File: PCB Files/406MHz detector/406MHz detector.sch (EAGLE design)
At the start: 17 parts, among them J1 switch

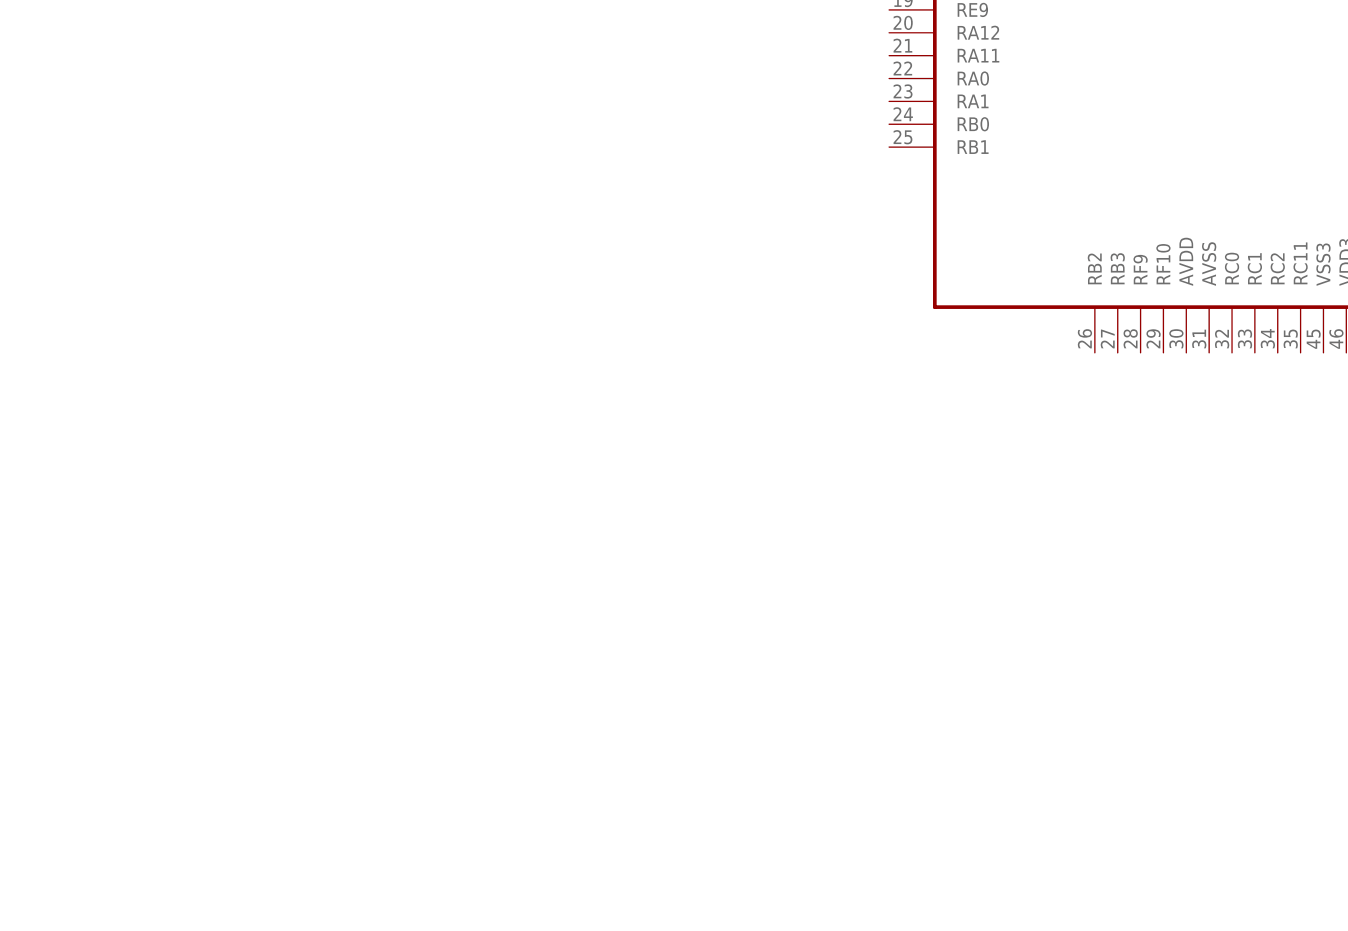
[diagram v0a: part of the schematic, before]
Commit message: added a microcontroller
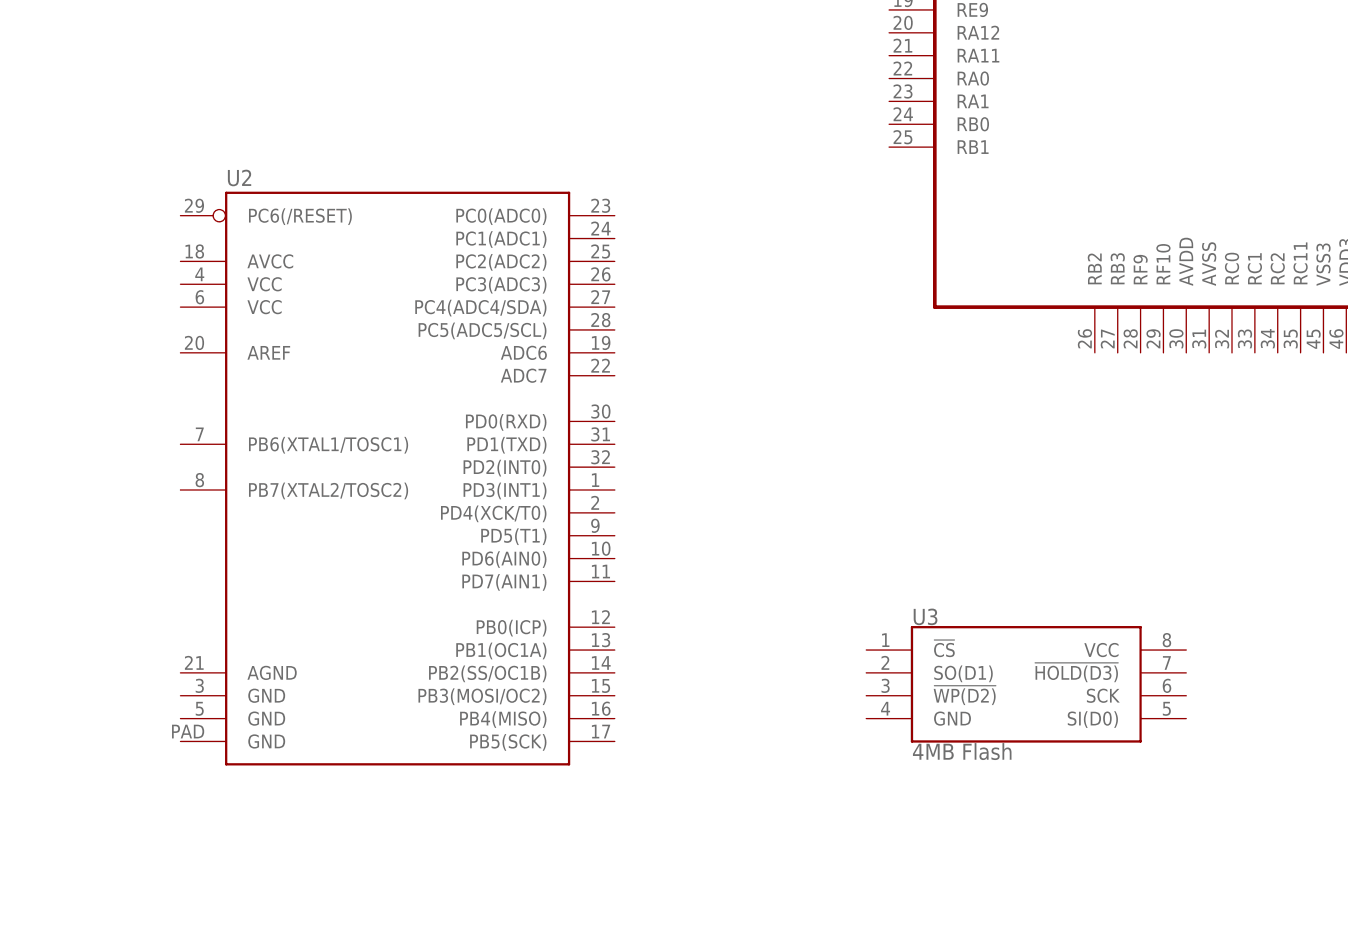
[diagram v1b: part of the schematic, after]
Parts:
- added U2: (no value), SparkFun-IC-Microcontroller:ATMEGA328P_MLFMLF32
- added U3: 4MB Flash, SparkFun-IC-Memory:AT25SF041
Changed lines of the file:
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@@
 <?xml version="1.0" encoding="utf-8"?>
 <!DOCTYPE eagle SYSTEM "eagle.dtd">
-<eagle version="9.3.0">
+<eagle version="9.5.2">
 <drawing>
 <settings>
@@
 <part name="GND6" library="SparkFun-PowerSymbols" library_urn="urn:adsk.eagle:library:530" deviceset="GND2" device="" value="GND"/>
 <part name="GND7" library="SparkFun-PowerSymbols" library_urn="urn:adsk.eagle:library:530" deviceset="GND2" device="" value="GND"/>
+<part name="U2" library="SparkFun-IC-Microcontroller" library_urn="urn:adsk.eagle:library:525" deviceset="ATMEGA328P_MLF" device="MLF32" package3d_urn="urn:adsk.eagle:package:38946/1"/>
+<part name="U3" library="SparkFun-IC-Memory" library_urn="urn:adsk.eagle:library:524" deviceset="AT25SF041" device="" package3d_urn="urn:adsk.eagle:package:38840/1" value="4MB Flash"/>
 </parts>
 <sheets>
@@
 <attribute name="VALUE" x="119.38" y="92.202" size="1.778" layer="96" align="top-center"/>
 </instance>
+<instance part="U2" gate="U$1" x="203.2" y="111.76" smashed="yes">
+<attribute name="NAME" x="185.42" y="140.462" size="1.778" layer="95"/>
+<attribute name="VALUE" x="185.42" y="73.66" size="1.778" layer="96"/>
+</instance>
+<instance part="U3" gate="G$1" x="271.78" y="83.82" smashed="yes">
+<attribute name="NAME" x="261.62" y="91.694" size="1.778" layer="95" font="vector"/>
+<attribute name="VALUE" x="261.62" y="78.486" size="1.778" layer="96" font="vector" align="top-left"/>
+</instance>
 </instances>

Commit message: added some nets
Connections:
- new net N$15: U2.PD0(RXD), U3.!CS
- new net N$16: U2.PD2(INT0), U3.!HOLD(D3), U3.SCK, U3.SI(D0), U3.VCC
- new net N$17: U2.GND@PAD, U3.GND
- new net N$18: U2.PB7(XTAL2/TOSC2), U3.SO(D1)
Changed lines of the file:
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@@
+</segment>
+</net>
+<net name="N$15" class="0">
+<segment>
+<pinref part="U2" gate="U$1" pin="PD0(RXD)"/>
+<pinref part="U3" gate="G$1" pin="!CS"/>
+<wire x1="228.6" y1="114.3" x2="256.54" y2="114.3" width="0.1524" layer="91"/>
+<wire x1="256.54" y1="114.3" x2="256.54" y2="88.9" width="0.1524" layer="91"/>
+</segment>
+</net>
+<net name="N$16" class="0">
+<segment>
+<pinref part="U2" gate="U$1" pin="PD2(INT0)"/>
+<pinref part="U3" gate="G$1" pin="SI(D0)"/>
+<wire x1="228.6" y1="109.22" x2="292.1" y2="109.22" width="0.1524" layer="91"/>
+<wire x1="292.1" y1="109.22" x2="292.1" y2="88.9" width="0.1524" layer="91"/>
+<pinref part="U3" gate="G$1" pin="VCC"/>
+<wire x1="292.1" y1="88.9" x2="292.1" y2="86.36" width="0.1524" layer="91"/>
+<junction x="292.1" y="88.9"/>
+<pinref part="U3" gate="G$1" pin="!HOLD(D3)"/>
+<wire x1="292.1" y1="86.36" x2="292.1" y2="83.82" width="0.1524" layer="91"/>
+<junction x="292.1" y="86.36"/>
+<pinref part="U3" gate="G$1" pin="SCK"/>
+<wire x1="292.1" y1="83.82" x2="292.1" y2="81.28" width="0.1524" layer="91"/>
+<junction x="292.1" y="83.82"/>
+</segment>
+</net>
+<net name="N$17" class="0">
+<segment>
+<pinref part="U3" gate="G$1" pin="GND"/>
+<wire x1="256.54" y1="81.28" x2="256.54" y2="63.5" width="0.1524" layer="91"/>
+<wire x1="256.54" y1="63.5" x2="180.34" y2="63.5" width="0.1524" layer="91"/>
+<pinref part="U2" gate="U$1" pin="GND@PAD"/>
+<wire x1="180.34" y1="63.5" x2="180.34" y2="78.74" width="0.1524" layer="91"/>
+</segment>
+</net>
+<net name="N$18" class="0">
+<segment>
+<pinref part="U2" gate="U$1" pin="PB7(XTAL2/TOSC2)"/>
+<wire x1="180.34" y1="106.68" x2="160.02" y2="106.68" width="0.1524" layer="91"/>
+<wire x1="160.02" y1="106.68" x2="160.02" y2="40.64" width="0.1524" layer="91"/>
+<wire x1="160.02" y1="40.64" x2="246.38" y2="40.64" width="0.1524" layer="91"/>
+<wire x1="246.38" y1="40.64" x2="246.38" y2="86.36" width="0.1524" layer="91"/>
+<pinref part="U3" gate="G$1" pin="SO(D1)"/>
+<wire x1="246.38" y1="86.36" x2="256.54" y2="86.36" width="0.1524" layer="91"/>
 </segment>
 </net>

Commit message: copied from master
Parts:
- removed U2: (no value), SparkFun-IC-Microcontroller:ATMEGA328P_MLFMLF32
- removed U3: 4MB Flash, SparkFun-IC-Memory:AT25SF041
- added D2: (no value), SparkFun-LED:LED_RING
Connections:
- net N$15: now also D2.1, D2.4; no longer U2.PD0(RXD), U3.!CS
- net N$16: now also D2.8, D2.9; no longer U2.PD2(INT0), U3.!HOLD(D3), U3.SCK, U3.SI(D0), U3.VCC
- net N$17: now also D2.12, D2.COM2; no longer U2.GND@PAD, U3.GND
- net N$18: now also D2.COM3; no longer U2.PB7(XTAL2/TOSC2), U3.SO(D1)
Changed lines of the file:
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@@
 <part name="GND6" library="SparkFun-PowerSymbols" library_urn="urn:adsk.eagle:library:530" deviceset="GND2" device="" value="GND"/>
 <part name="GND7" library="SparkFun-PowerSymbols" library_urn="urn:adsk.eagle:library:530" deviceset="GND2" device="" value="GND"/>
-<part name="U2" library="SparkFun-IC-Microcontroller" library_urn="urn:adsk.eagle:library:525" deviceset="ATMEGA328P_MLF" device="MLF32" package3d_urn="urn:adsk.eagle:package:38946/1"/>
-<part name="U3" library="SparkFun-IC-Memory" library_urn="urn:adsk.eagle:library:524" deviceset="AT25SF041" device="" package3d_urn="urn:adsk.eagle:package:38840/1" value="4MB Flash"/>
+<part name="D2" library="SparkFun-LED" library_urn="urn:adsk.eagle:library:529" deviceset="LED_RING" device="" package3d_urn="urn:adsk.eagle:package:39360/1"/>
 </parts>
 <sheets>
 <sheet>
 <plain>
+<wire x1="0" y1="0" x2="0" y2="381" width="0.1524" layer="150"/>
+<wire x1="0" y1="381" x2="508" y2="381" width="0.1524" layer="150"/>
+<wire x1="508" y1="381" x2="508" y2="0" width="0.1524" layer="150"/>
+<wire x1="508" y1="0" x2="0" y2="0" width="0.1524" layer="150"/>
+<wire x1="508" y1="381" x2="1016" y2="381" width="0.1524" layer="150"/>
+<wire x1="1016" y1="381" x2="1016" y2="0" width="0.1524" layer="150"/>
+<wire x1="1016" y1="0" x2="508" y2="0" width="0.1524" layer="150"/>
+<wire x1="1016" y1="381" x2="1524" y2="381" width="0.1524" layer="150"/>
+<wire x1="1524" y1="381" x2="1524" y2="0" width="0.1524" layer="150"/>
+<wire x1="1524" y1="0" x2="1016" y2="0" width="0.1524" layer="150"/>
 </plain>
 <instances>
@@
 <attribute name="VALUE" x="119.38" y="92.202" size="1.778" layer="96" align="top-center"/>
 </instance>
-<instance part="U2" gate="U$1" x="203.2" y="111.76" smashed="yes">
-<attribute name="NAME" x="185.42" y="140.462" size="1.778" layer="95"/>
-<attribute name="VALUE" x="185.42" y="73.66" size="1.778" layer="96"/>
-</instance>
-<instance part="U3" gate="G$1" x="271.78" y="83.82" smashed="yes">
-<attribute name="NAME" x="261.62" y="91.694" size="1.778" layer="95" font="vector"/>
-<attribute name="VALUE" x="261.62" y="78.486" size="1.778" layer="96" font="vector" align="top-left"/>
+<instance part="D2" gate="G$1" x="193.04" y="96.52" smashed="yes">
+<attribute name="VALUE" x="193.04" y="81.026" size="1.778" layer="96" font="vector" align="top-center"/>
+<attribute name="NAME" x="193.04" y="112.014" size="1.778" layer="95" font="vector" align="bottom-center"/>
 </instance>
 </instances>
@@
 <net name="N$15" class="0">
 <segment>
-<pinref part="U2" gate="U$1" pin="PD0(RXD)"/>
-<pinref part="U3" gate="G$1" pin="!CS"/>
-<wire x1="228.6" y1="114.3" x2="256.54" y2="114.3" width="0.1524" layer="91"/>
-<wire x1="256.54" y1="114.3" x2="256.54" y2="88.9" width="0.1524" layer="91"/>
+<pinref part="D2" gate="G$1" pin="1"/>
+<wire x1="177.8" y1="99.06" x2="167.64" y2="99.06" width="0.1524" layer="91"/>
+<wire x1="167.64" y1="99.06" x2="167.64" y2="109.22" width="0.1524" layer="91"/>
+<pinref part="D2" gate="G$1" pin="4"/>
+<wire x1="167.64" y1="109.22" x2="177.8" y2="109.22" width="0.1524" layer="91"/>
 </segment>
 </net>
 <net name="N$16" class="0">
 <segment>
-<pinref part="U2" gate="U$1" pin="PD2(INT0)"/>
-<pinref part="U3" gate="G$1" pin="SI(D0)"/>
-<wire x1="228.6" y1="109.22" x2="292.1" y2="109.22" width="0.1524" layer="91"/>
-<wire x1="292.1" y1="109.22" x2="292.1" y2="88.9" width="0.1524" layer="91"/>
-<pinref part="U3" gate="G$1" pin="VCC"/>
-<wire x1="292.1" y1="88.9" x2="292.1" y2="86.36" width="0.1524" layer="91"/>
-<junction x="292.1" y="88.9"/>
-<pinref part="U3" gate="G$1" pin="!HOLD(D3)"/>
-<wire x1="292.1" y1="86.36" x2="292.1" y2="83.82" width="0.1524" layer="91"/>
-<junction x="292.1" y="86.36"/>
-<pinref part="U3" gate="G$1" pin="SCK"/>
-<wire x1="292.1" y1="83.82" x2="292.1" y2="81.28" width="0.1524" layer="91"/>
-<junction x="292.1" y="83.82"/>
+<pinref part="D2" gate="G$1" pin="9"/>
+<wire x1="208.28" y1="93.98" x2="215.9" y2="93.98" width="0.1524" layer="91"/>
+<pinref part="D2" gate="G$1" pin="8"/>
+<wire x1="215.9" y1="93.98" x2="215.9" y2="99.06" width="0.1524" layer="91"/>
+<wire x1="215.9" y1="99.06" x2="208.28" y2="99.06" width="0.1524" layer="91"/>
 </segment>
 </net>
 <net name="N$17" class="0">
 <segment>
-<pinref part="U3" gate="G$1" pin="GND"/>
-<wire x1="256.54" y1="81.28" x2="256.54" y2="63.5" width="0.1524" layer="91"/>
-<wire x1="256.54" y1="63.5" x2="180.34" y2="63.5" width="0.1524" layer="91"/>
-<pinref part="U2" gate="U$1" pin="GND@PAD"/>
-<wire x1="180.34" y1="63.5" x2="180.34" y2="78.74" width="0.1524" layer="91"/>
+<pinref part="D2" gate="G$1" pin="12"/>
+<pinref part="D2" gate="G$1" pin="COM2"/>
+<wire x1="223.52" y1="83.82" x2="208.28" y2="83.82" width="0.1524" layer="91"/>
+<wire x1="208.28" y1="83.82" x2="208.28" y2="81.28" width="0.1524" layer="91"/>
 </segment>
 </net>
 <net name="N$18" class="0">
 <segment>
-<pinref part="U2" gate="U$1" pin="PB7(XTAL2/TOSC2)"/>
-<wire x1="180.34" y1="106.68" x2="160.02" y2="106.68" width="0.1524" layer="91"/>
-<wire x1="160.02" y1="106.68" x2="160.02" y2="40.64" width="0.1524" layer="91"/>
-<wire x1="160.02" y1="40.64" x2="246.38" y2="40.64" width="0.1524" layer="91"/>
-<wire x1="246.38" y1="40.64" x2="246.38" y2="86.36" width="0.1524" layer="91"/>
-<pinref part="U3" gate="G$1" pin="SO(D1)"/>
-<wire x1="246.38" y1="86.36" x2="256.54" y2="86.36" width="0.1524" layer="91"/>
-</segment>
-</net>
+<pinref part="D2" gate="G$1" pin="COM3"/>
+<wire x1="177.8" y1="81.28" x2="165.1" y2="81.28" width="0.1524" layer="91"/>
+</segment>
+</net>
